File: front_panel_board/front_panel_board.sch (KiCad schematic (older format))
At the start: 9 parts, among them J1 Molex_SL_01x02_Male, J2 Conn_02x05_Odd_Even, J3 Conn_02x05_Odd_Even, SW1 SW_Rotary8_CK_A125xxxxCxx, SW2 SW_SPDT

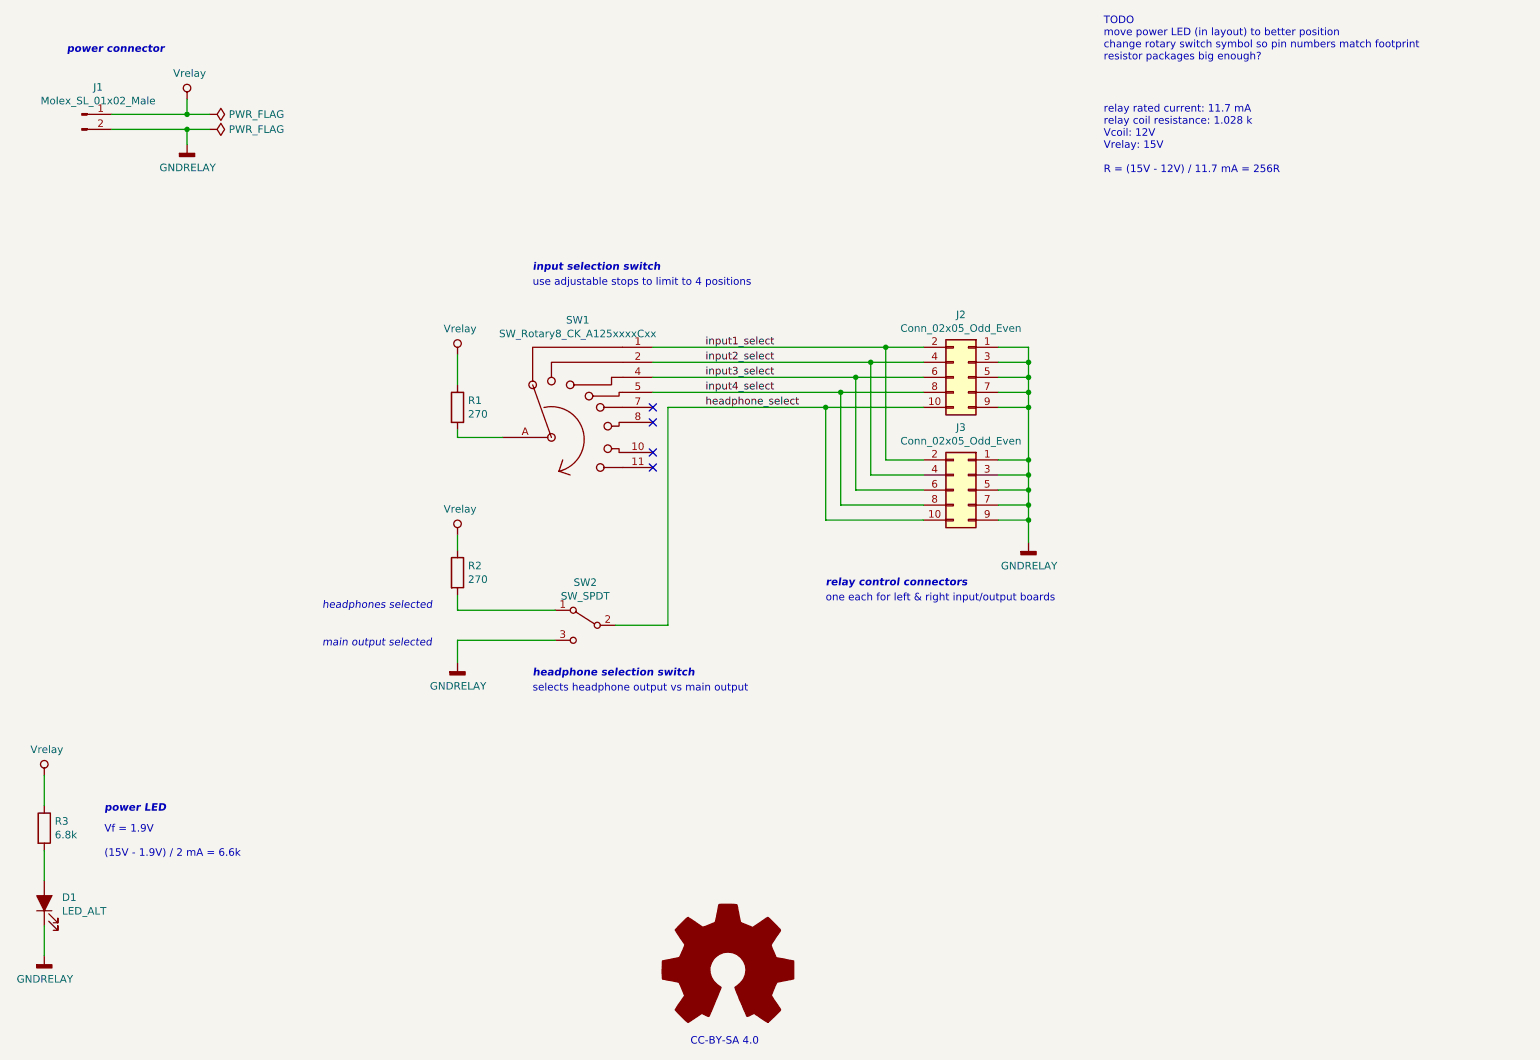
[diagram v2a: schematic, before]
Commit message: change relay resistors to 0805 and label headphone switch
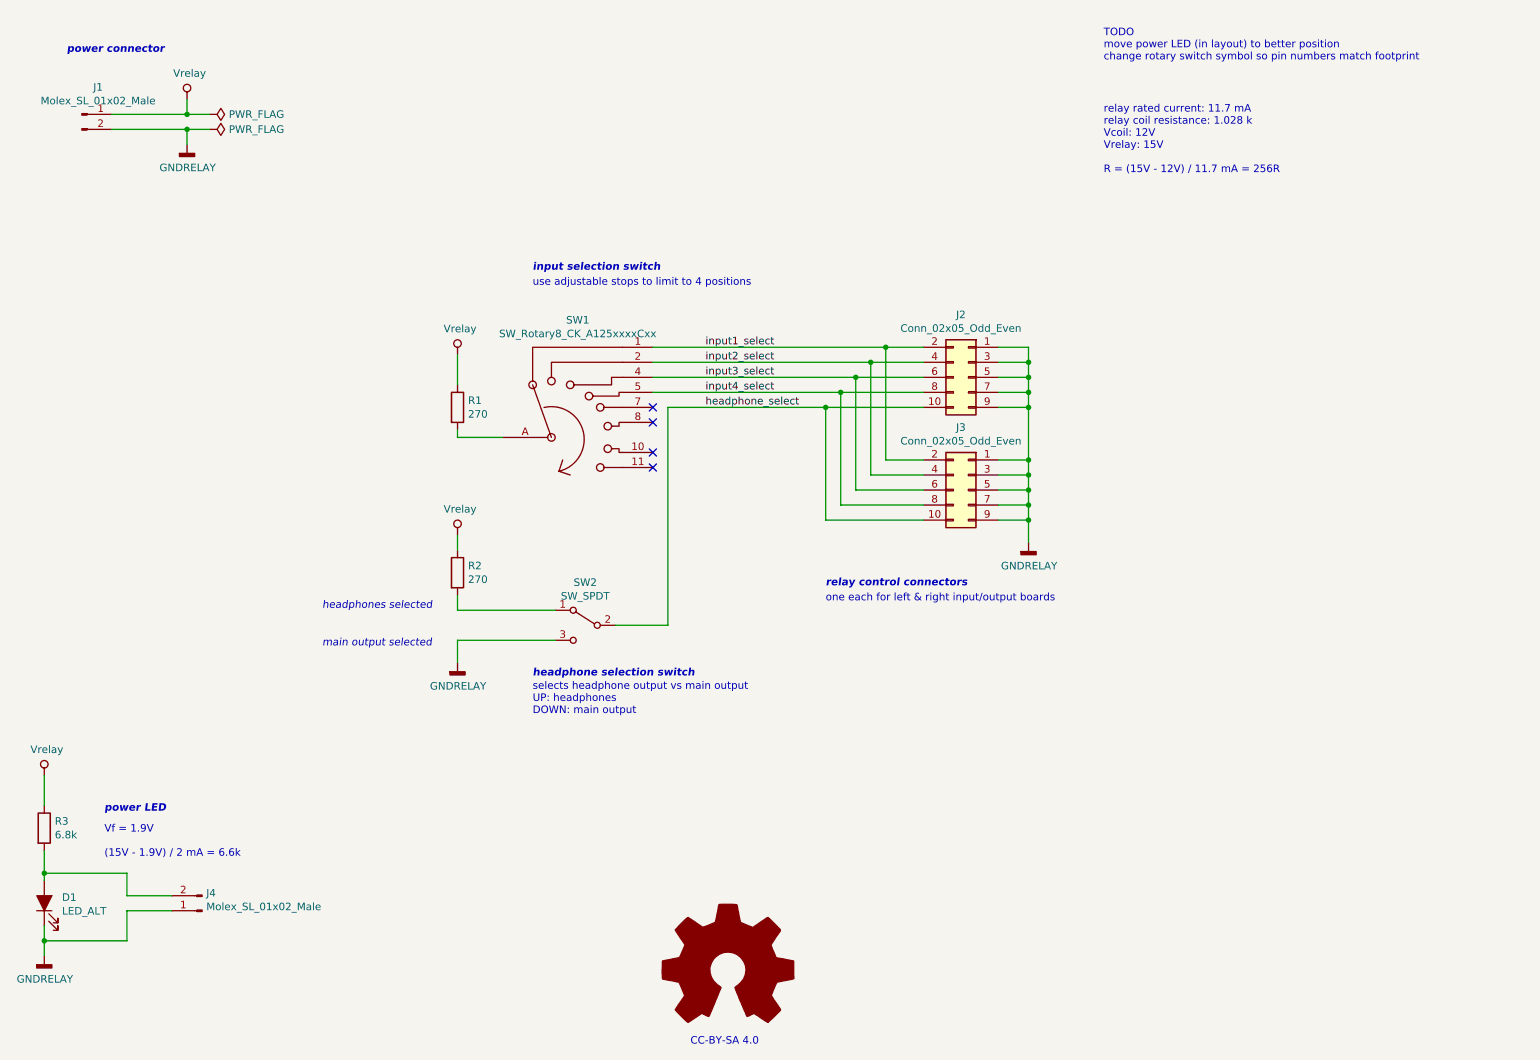
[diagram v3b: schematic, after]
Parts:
- added J4: Molex_SL_01x02_Male, Connector_Molex_SL:Molex_SL_A-70543-0001_1x02_P2.54mm_Vertical, symbol Connector_gkeeth:Molex_SL_01x02_Male
- R1, R2: footprint Resistor_SMD:R_0603_1608Metric_Pad1.05x0.95mm_HandSolder -> Resistor_SMD:R_0805_2012Metric_Pad1.15x1.40mm_HandSolder; Distributor Digikey -> (none); Distributor PN 311-2504-1-ND -> (none); Manufacturer Yageo -> (none); Manufacturer PN RT0603DRE07270RL -> (none); URL https://www.digikey.com/product-detail/en/yageo/RT0603DRE07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 -> (none); Unit Price 0.12 -> (none)
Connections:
- net GNDRELAY: now also J4.1 (Pin_1)
- net at D1.2 (A), R3.2: now also J4.2 (Pin_2)
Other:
- note added: "TODO\nmove power LED (in layout) to better position\nchange rotary switch symbol so pin numbers match footprint"
- note added: "selects headphone output vs main output\nUP: headphones\nDOWN: main output"
- note removed: "TODO\nmove power LED (in layout) to better position\nchange rotary switch symbol so pin numbers match footprint\nresistor packages big enough?"
- note removed: "selects headphone output vs main output"
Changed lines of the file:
@@
-	1    0    0    -1
-$EndComp
-$Comp
-L Device:R R1
-U 1 1 5CD3055D
-P 3700 3400
-F 0 "R1" H 3770 3446 50  0000 L CNN
-F 1 "270" H 3770 3355 50  0000 L CNN
-F 2 "Resistor_SMD:R_0603_1608Metric_Pad1.05x0.95mm_HandSolder" V 3630 3400 50  0001 C CNN
-F 3 "http://www.yageo.com/documents/recent/PYu-RT_1-to-0.01_RoHS_L_9.pdf" H 3700 3400 50  0001 C CNN
-F 4 "Yageo" H 3700 3400 50  0001 C CNN "Manufacturer"
-F 5 "RT0603DRE07270RL" H 3700 3400 50  0001 C CNN "Manufacturer PN"
-F 6 "Digikey" H 3700 3400 50  0001 C CNN "Distributor"
-F 7 "311-2504-1-ND" H 3700 3400 50  0001 C CNN "Distributor PN"
-F 8 "https://www.digikey.com/product-detail/en/yageo/RT0603DRE07270RL/311-2504-1-ND/6128923" H 3700 3400 50  0001 C CNN "URL"
-F 9 "0.12" H 3700 3400 50  0001 C CNN "Unit Price"
-	1    3700 3400
 	1    0    0    -1
 $EndComp
@@
 Wire Wire Line
 	3700 4350 3700 4250
-Text Notes 4200 5300 0    50   ~ 0
-selects headphone output vs main output
+Text Notes 4200 5450 0    50   ~ 0
+selects headphone output vs main output\nUP: headphones\nDOWN: main output
 Text Notes 4200 5200 0    50   Italic 10
 headphone selection switch
@@
 input selection switch
 Wire Wire Line
-	950  6350 950  6550
+	950  6350 950  6500
 $Comp
 L power_gkeeth:GNDRELAY #PWR0106
@@
 $EndComp
 Wire Wire Line
-	950  7050 950  6850
+	950  7050 950  6950
 $Comp
 L power_gkeeth:Vrelay #PWR0107
@@
 F 0 "R2" H 3770 4546 50  0000 L CNN
 F 1 "270" H 3770 4455 50  0000 L CNN
-F 2 "Resistor_SMD:R_0603_1608Metric_Pad1.05x0.95mm_HandSolder" V 3630 4500 50  0001 C CNN
-F 3 "http://www.yageo.com/documents/recent/PYu-RT_1-to-0.01_RoHS_L_9.pdf" H 3700 4500 50  0001 C CNN
-F 4 "Yageo" H 3700 4500 50  0001 C CNN "Manufacturer"
-F 5 "RT0603DRE07270RL" H 3700 4500 50  0001 C CNN "Manufacturer PN"
-F 6 "Digikey" H 3700 4500 50  0001 C CNN "Distributor"
-F 7 "311-2504-1-ND" H 3700 4500 50  0001 C CNN "Distributor PN"
-F 8 "https://www.digikey.com/product-detail/en/yageo/RT0603DRE07270RL/311-2504-1-ND/6128923" H 3700 4500 50  0001 C CNN "URL"
-F 9 "0.12" H 3700 4500 50  0001 C CNN "Unit Price"
+F 2 "Resistor_SMD:R_0805_2012Metric_Pad1.15x1.40mm_HandSolder" V 3630 4500 50  0001 C CNN
+F 3 "" H 3700 4500 50  0001 C CNN
 	1    3700 4500
 	1    0    0    -1
@@
 Vf = 1.9V\n\n(15V - 1.9V) / 2 mA = 6.6k
 Text Notes 8000 1100 0    50   ~ 0
-TODO\nmove power LED (in layout) to better position\nchange rotary switch symbol so pin numbers match footprint\nresistor packages big enough?
+TODO\nmove power LED (in layout) to better position\nchange rotary switch symbol so pin numbers match footprint
 $Comp
 L Graphic:Logo_Open_Hardware_Large #LOGO1
@@
 Text Notes 2800 5000 0    50   Italic 0
 main output selected
+$Comp
+L Connector_gkeeth:Molex_SL_01x02_Male J4
+U 1 1 5D95AB4A
+P 2000 6750
+F 0 "J4" H 1972 6632 50  0000 R CNN
+F 1 "Molex_SL_01x02_Male" H 1972 6723 50  0000 R CNN
+F 2 "Connector_Molex_SL:Molex_SL_A-70543-0001_1x02_P2.54mm_Vertical" H 2000 6750 50  0001 C CNN
+F 3 "https://www.molex.com/pdm_docs/sd/705430001_sd.pdf" H 2000 6750 50  0001 C CNN
+	1    2000 6750
+	-1   0    0    1
+$EndComp
+Wire Wire Line
+	1500 6650 1500 6500
+Wire Wire Line
+	1500 6500 950  6500
+Wire Wire Line
+	1500 6650 1800 6650
+Connection ~ 950  6500
+Wire Wire Line
+	950  6500 950  6550
+Wire Wire Line
+	950  6950 1500 6950
+Wire Wire Line
+	1500 6950 1500 6750
+Wire Wire Line
+	1500 6750 1800 6750
+Connection ~ 950  6950
+Wire Wire Line
+	950  6950 950  6850
+$Comp
+L Device:R R1
+U 1 1 5D940B78
+P 3700 3400
+F 0 "R1" H 3770 3446 50  0000 L CNN
+F 1 "270" H 3770 3355 50  0000 L CNN
+F 2 "Resistor_SMD:R_0805_2012Metric_Pad1.15x1.40mm_HandSolder" V 3630 3400 50  0001 C CNN
+F 3 "" H 3700 3400 50  0001 C CNN
+	1    3700 3400
+	1    0    0    -1
+$EndComp
 $EndSCHEMATC

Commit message: complete all BOM info
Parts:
- J1, J4: Distributor (none) -> Digikey; Distributor PN (none) -> WM4800-ND; Manufacturer (none) -> Molex; Manufacturer PN (none) -> 0705430001; URL (none) -> https://www.molex.com/pdm_docs/sd/705430001_sd.pdf; Unit Price (none) -> 0.84
- J2, J3: Distributor (none) -> Digikey; Distributor PN (none) -> WM9219-ND; Manufacturer (none) -> Molex; Manufacturer PN (none) -> 0702461001; URL (none) -> https://www.digikey.com/products/en?keywords=70246-1001; Unit Price (none) -> 1.70
- R1, R2: Distributor (none) -> Mouser; Distributor PN (none) -> 603-RT0805FRE07270RL; Manufacturer (none) -> Yageo; Manufacturer PN (none) -> RT0805FRE07270RL; URL (none) -> https://www.mouser.com/ProductDetail/603-RT0805FRE07270RL; Unit Price (none) -> 0.12
- SW1: Distributor (none) -> Mouser; Distributor PN (none) -> 611-A12505RNCQ; Manufacturer (none) -> C&K; Manufacturer PN (none) -> A12505RNCQ; URL (none) -> https://www.mouser.com/ProductDetail/611-A12505RNCQ; Unit Price (none) -> 8.05
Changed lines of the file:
@@
 F 1 "270" H 3770 4455 50  0000 L CNN
 F 2 "Resistor_SMD:R_0805_2012Metric_Pad1.15x1.40mm_HandSolder" V 3630 4500 50  0001 C CNN
-F 3 "" H 3700 4500 50  0001 C CNN
+F 3 "https://www.mouser.com/datasheet/2/447/PYu-RT_1-to-0.01_RoHS_L_9-1222720.pdf" H 3700 4500 50  0001 C CNN
+F 4 "603-RT0805FRE07270RL" H 3700 4500 50  0001 C CNN "Distributor PN"
+F 5 "Mouser" H 3700 4500 50  0001 C CNN "Distributor"
+F 6 "Yageo" H 3700 4500 50  0001 C CNN "Manufacturer"
+F 7 "RT0805FRE07270RL" H 3700 4500 50  0001 C CNN "Manufacturer PN"
+F 8 "https://www.mouser.com/ProductDetail/603-RT0805FRE07270RL" H 3700 4500 50  0001 C CNN "URL"
+F 9 "0.12" H 3700 4500 50  0001 C CNN "Unit Price"
 	1    3700 4500
 	1    0    0    -1
@@
 F 2 "Connector_Molex_SL:Molex_SL_A-70543-0001_1x02_P2.54mm_Vertical" H 1200 1450 50  0001 C CNN
 F 3 "https://www.molex.com/pdm_docs/sd/705430001_sd.pdf" H 1200 1450 50  0001 C CNN
+F 4 "Digikey" H 1200 1450 50  0001 C CNN "Distributor"
+F 5 "WM4800-ND" H 1200 1450 50  0001 C CNN "Distributor PN"
+F 6 "Molex" H 1200 1450 50  0001 C CNN "Manufacturer"
+F 7 "0705430001" H 1200 1450 50  0001 C CNN "Manufacturer PN"
+F 8 "https://www.molex.com/pdm_docs/sd/705430001_sd.pdf" H 1200 1450 50  0001 C CNN "URL"
+F 9 "0.84" H 1200 1450 50  0001 C CNN "Unit Price"
 	1    1200 1450
 	1    0    0    -1
@@
 F 2 "Button_Switch_THT_gkeeth:SW_Rotary8_CK_A125xxxxCxx" H 4400 4300 50  0001 C CNN
 F 3 "https://www.ckswitches.com/media/1349/arotary.pdf" H 4400 4300 50  0001 C CNN
+F 4 "Mouser" H 4600 3600 50  0001 C CNN "Distributor"
+F 5 "611-A12505RNCQ" H 4600 3600 50  0001 C CNN "Distributor PN"
+F 6 "C&K" H 4600 3600 50  0001 C CNN "Manufacturer"
+F 7 "A12505RNCQ" H 4600 3600 50  0001 C CNN "Manufacturer PN"
+F 8 "https://www.mouser.com/ProductDetail/611-A12505RNCQ" H 4600 3600 50  0001 C CNN "URL"
+F 9 "8.05" H 4600 3600 50  0001 C CNN "Unit Price"
 	1    4600 3600
 	1    0    0    -1
@@
 F 1 "Conn_02x05_Odd_Even" H 7150 4276 50  0000 C CNN
 F 2 "Connector_Molex_C-Grid:Molex_C-Grid_70246-1001_2x05_P2.54mm_Vertical" H 7100 3950 50  0001 C CNN
-F 3 "~" H 7100 3950 50  0001 C CNN
+F 3 "https://www.molex.com/pdm_docs/sd/702461001_sd.pdf" H 7100 3950 50  0001 C CNN
+F 4 "Digikey" H 7100 3950 50  0001 C CNN "Distributor"
+F 5 "WM9219-ND" H 7100 3950 50  0001 C CNN "Distributor PN"
+F 6 "Molex" H 7100 3950 50  0001 C CNN "Manufacturer"
+F 7 "0702461001" H 7100 3950 50  0001 C CNN "Manufacturer PN"
+F 8 "https://www.digikey.com/products/en?keywords=70246-1001" H 7100 3950 50  0001 C CNN "URL"
+F 9 "1.70" H 7100 3950 50  0001 C CNN "Unit Price"
 	1    7100 3950
 	-1   0    0    -1
@@
 F 1 "Conn_02x05_Odd_Even" H 7150 3526 50  0000 C CNN
 F 2 "Connector_Molex_C-Grid:Molex_C-Grid_70246-1001_2x05_P2.54mm_Vertical" H 7100 3200 50  0001 C CNN
-F 3 "~" H 7100 3200 50  0001 C CNN
+F 3 "https://www.molex.com/pdm_docs/sd/702461001_sd.pdf" H 7100 3200 50  0001 C CNN
+F 4 "Digikey" H 7100 3200 50  0001 C CNN "Distributor"
+F 5 "WM9219-ND" H 7100 3200 50  0001 C CNN "Distributor PN"
+F 6 "Molex" H 7100 3200 50  0001 C CNN "Manufacturer"
+F 7 "0702461001" H 7100 3200 50  0001 C CNN "Manufacturer PN"
+F 8 "https://www.digikey.com/products/en?keywords=70246-1001" H 7100 3200 50  0001 C CNN "URL"
+F 9 "1.70" H 7100 3200 50  0001 C CNN "Unit Price"
 	1    7100 3200
 	-1   0    0    -1
@@
 F 2 "Connector_Molex_SL:Molex_SL_A-70543-0001_1x02_P2.54mm_Vertical" H 2000 6750 50  0001 C CNN
 F 3 "https://www.molex.com/pdm_docs/sd/705430001_sd.pdf" H 2000 6750 50  0001 C CNN
+F 4 "Digikey" H 2000 6750 50  0001 C CNN "Distributor"
+F 5 "WM4800-ND" H 2000 6750 50  0001 C CNN "Distributor PN"
+F 6 "Molex" H 2000 6750 50  0001 C CNN "Manufacturer"
+F 7 "0705430001" H 2000 6750 50  0001 C CNN "Manufacturer PN"
+F 8 "https://www.molex.com/pdm_docs/sd/705430001_sd.pdf" H 2000 6750 50  0001 C CNN "URL"
+F 9 "0.84" H 2000 6750 50  0001 C CNN "Unit Price"
 	1    2000 6750
 	-1   0    0    1
@@
 F 1 "270" H 3770 3355 50  0000 L CNN
 F 2 "Resistor_SMD:R_0805_2012Metric_Pad1.15x1.40mm_HandSolder" V 3630 3400 50  0001 C CNN
-F 3 "" H 3700 3400 50  0001 C CNN
+F 3 "https://www.mouser.com/datasheet/2/447/PYu-RT_1-to-0.01_RoHS_L_9-1222720.pdf" H 3700 3400 50  0001 C CNN
+F 4 "603-RT0805FRE07270RL" H 3700 3400 50  0001 C CNN "Distributor PN"
+F 5 "Mouser" H 3700 3400 50  0001 C CNN "Distributor"
+F 6 "Yageo" H 3700 3400 50  0001 C CNN "Manufacturer"
+F 7 "RT0805FRE07270RL" H 3700 3400 50  0001 C CNN "Manufacturer PN"
+F 8 "https://www.mouser.com/ProductDetail/603-RT0805FRE07270RL" H 3700 3400 50  0001 C CNN "URL"
+F 9 "0.12" H 3700 3400 50  0001 C CNN "Unit Price"
 	1    3700 3400
 	1    0    0    -1
